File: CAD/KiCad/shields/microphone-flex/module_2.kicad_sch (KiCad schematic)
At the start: 1 part, among them J3 RIGHT / 1x05 RIGHT ANGLE

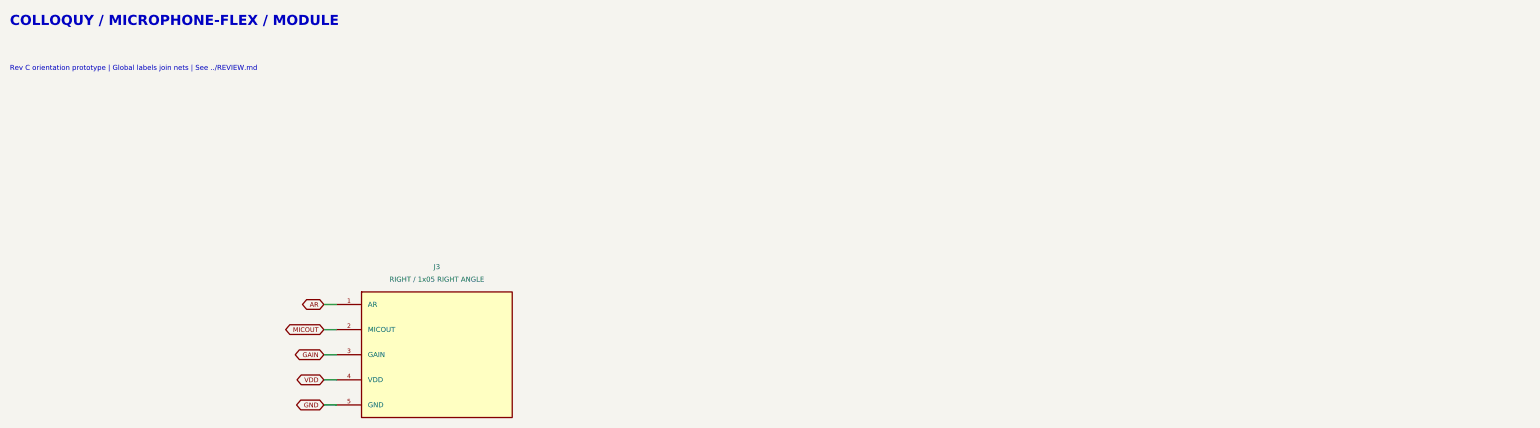
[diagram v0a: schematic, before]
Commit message: Restore removable microphone gain and A/R selectors across flex design
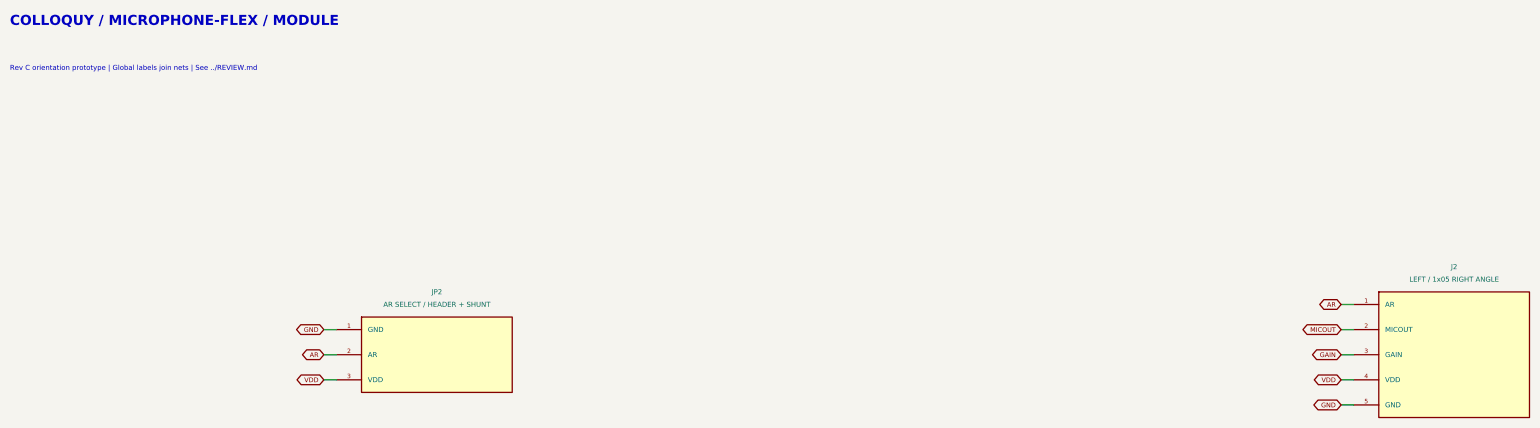
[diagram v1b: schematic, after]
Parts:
- removed J3: RIGHT / 1x05 RIGHT ANGLE, Shields:Flex_Socket_Side, symbol Colloquy:J3
- added J2: LEFT / 1x05 RIGHT ANGLE, Shields:Flex_Socket_Side, symbol Colloquy:J2
- added JP2: AR SELECT / HEADER + SHUNT, Shields:Flex_AR_Selector, symbol Colloquy:JP2
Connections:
- net AR: now also J2.1 (AR), JP2.2 (AR)
- net GAIN: now also J2.3 (GAIN)
- net GND: now also J2.5 (GND), JP2.1 (GND)
- net MICOUT: now also J2.2 (MICOUT)
- net VDD: now also J2.4 (VDD), JP2.3 (VDD)
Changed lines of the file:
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@@
 (kicad_sch (version 20250114) (generator "eeschema") (generator_version "9.0")
  (paper "A3")
-          (title_block (title "microphone-flex / module") (date "2026-10-05") (rev "A-prototype")
+          (title_block (title "microphone-flex / module") (date "2026-10-20") (rev "C-jumpers")
             (company "Colloquy of Mobiles") (comment 1 "Prototype: verify harness polarity and sensor values before connection"))
           (text "COLLOQUY / MICROPHONE-FLEX / MODULE" (at 15.24 15.24 0) (effects (font (size 2.032 2.032) (bold yes)) (justify left top)))
 (text "Rev C orientation prototype | Global labels join nets | See ../REVIEW.md" (at 15.24 25.4 0) (effects (font (size 1.016 1.016) ) (justify left top)))
-(symbol (lib_id "Colloquy:J3") (at 101.6000 83.8200 0) (unit 1) (exclude_from_sim no) (in_bom yes) (on_board yes) (dnp no)
-(property "Reference" "J3" (at 101.6000 66.0400 0) (effects (font (size 1.016 1.016))  ))
-(property "Value" "RIGHT / 1x05 RIGHT ANGLE" (at 101.6000 68.5800 0) (effects (font (size 1.016 1.016))  ))
-(property "Footprint" "Shields:Flex_Socket_Side" (at 101.6000 83.8200 0) (effects (font (size 1.27 1.27))  (hide yes)))
+(symbol (lib_id "Colloquy:JP2") (at 101.6000 83.8200 0) (unit 1) (exclude_from_sim no) (in_bom yes) (on_board yes) (dnp no)
+(property "Reference" "JP2" (at 101.6000 71.1200 0) (effects (font (size 1.016 1.016))  ))
+(property "Value" "AR SELECT / HEADER + SHUNT" (at 101.6000 73.6600 0) (effects (font (size 1.016 1.016))  ))
+(property "Footprint" "Shields:Flex_AR_Selector" (at 101.6000 83.8200 0) (effects (font (size 1.27 1.27))  (hide yes)))
 (property "Datasheet" "" (at 101.6000 83.8200 0) (effects (font (size 1.27 1.27))  (hide yes)))
-(property "Description" "Alternative socket; AR / Out / Gain / Vdd / GND in physical pad order. One module only." (at 101.6000 83.8200 0) (effects (font (size 1.27 1.27))  (hide yes)))
+(property "Description" "Removable 2.54mm selector. 1-2:1:500; 2-3:1:2000; open:1:4000. Initially 1-2. Power off before moving the shunt." (at 101.6000 83.8200 0) (effects (font (size 1.27 1.27))  (hide yes)))
+(pin "1")
+(pin "2")
+(pin "3")
+(instances (project "microphone-flex" (path "/767eeb75-0bc5-5c78-a7ae-aa35b79c1dd4/2d8114f0-91f1-5f81-b7b6-783b8e2a941e" (reference "JP2") (unit 1)))))
+(wire (pts (xy 81.2800 78.7400) (xy 78.7400 78.7400)) (stroke (width 0) (type default)))
+(global_label "GND" (shape bidirectional) (at 78.7400 78.7400 180) (effects (font (size 0.95 0.95)) (justify right)) (property "Intersheetrefs" "${INTERSHEET_REFS}" (at 78.7400 78.7400 0) (effects (font (size 1.016 1.016))  (hide yes))))
+(wire (pts (xy 81.2800 83.8200) (xy 78.7400 83.8200)) (stroke (width 0) (type default)))
+(global_label "AR" (shape bidirectional) (at 78.7400 83.8200 180) (effects (font (size 0.95 0.95)) (justify right)) (property "Intersheetrefs" "${INTERSHEET_REFS}" (at 78.7400 83.8200 0) (effects (font (size 1.016 1.016))  (hide yes))))
+(wire (pts (xy 81.2800 88.9000) (xy 78.7400 88.9000)) (stroke (width 0) (type default)))
+(global_label "VDD" (shape bidirectional) (at 78.7400 88.9000 180) (effects (font (size 0.95 0.95)) (justify right)) (property "Intersheetrefs" "${INTERSHEET_REFS}" (at 78.7400 88.9000 0) (effects (font (size 1.016 1.016))  (hide yes))))
+(symbol (lib_id "Colloquy:J2") (at 307.3400 83.8200 0) (unit 1) (exclude_from_sim no) (in_bom yes) (on_board yes) (dnp no)
+(property "Reference" "J2" (at 307.3400 66.0400 0) (effects (font (size 1.016 1.016))  ))
+(property "Value" "LEFT / 1x05 RIGHT ANGLE" (at 307.3400 68.5800 0) (effects (font (size 1.016 1.016))  ))
+(property "Footprint" "Shields:Flex_Socket_Side" (at 307.3400 83.8200 0) (effects (font (size 1.27 1.27))  (hide yes)))
+(property "Datasheet" "" (at 307.3400 83.8200 0) (effects (font (size 1.27 1.27))  (hide yes)))
+(property "Description" "Alternative socket; AR / Out / Gain / Vdd / GND in physical pad order. One module only." (at 307.3400 83.8200 0) (effects (font (size 1.27 1.27))  (hide yes)))
 (pin "1")
 (pin "2")
@@
 (pin "4")
 (pin "5")
-(instances (project "microphone-flex" (path "/767eeb75-0bc5-5c78-a7ae-aa35b79c1dd4/2d8114f0-91f1-5f81-b7b6-783b8e2a941e" (reference "J3") (unit 1)))))
-(wire (pts (xy 81.2800 73.6600) (xy 78.7400 73.6600)) (stroke (width 0) (type default)))
-(global_label "AR" (shape bidirectional) (at 78.7400 73.6600 180) (effects (font (size 0.95 0.95)) (justify right)) (property "Intersheetrefs" "${INTERSHEET_REFS}" (at 78.7400 73.6600 0) (effects (font (size 1.016 1.016))  (hide yes))))
-(wire (pts (xy 81.2800 78.7400) (xy 78.7400 78.7400)) (stroke (width 0) (type default)))
-(global_label "MICOUT" (shape bidirectional) (at 78.7400 78.7400 180) (effects (font (size 0.95 0.95)) (justify right)) (property "Intersheetrefs" "${INTERSHEET_REFS}" (at 78.7400 78.7400 0) (effects (font (size 1.016 1.016))  (hide yes))))
-(wire (pts (xy 81.2800 83.8200) (xy 78.7400 83.8200)) (stroke (width 0) (type default)))
-(global_label "GAIN" (shape bidirectional) (at 78.7400 83.8200 180) (effects (font (size 0.95 0.95)) (justify right)) (property "Intersheetrefs" "${INTERSHEET_REFS}" (at 78.7400 83.8200 0) (effects (font (size 1.016 1.016))  (hide yes))))
-(wire (pts (xy 81.2800 88.9000) (xy 78.7400 88.9000)) (stroke (width 0) (type default)))
-(global_label "VDD" (shape bidirectional) (at 78.7400 88.9000 180) (effects (font (size 0.95 0.95)) (justify right)) (property "Intersheetrefs" "${INTERSHEET_REFS}" (at 78.7400 88.9000 0) (effects (font (size 1.016 1.016))  (hide yes))))
-(wire (pts (xy 81.2800 93.9800) (xy 78.7400 93.9800)) (stroke (width 0) (type default)))
-(global_label "GND" (shape bidirectional) (at 78.7400 93.9800 180) (effects (font (size 0.95 0.95)) (justify right)) (property "Intersheetrefs" "${INTERSHEET_REFS}" (at 78.7400 93.9800 0) (effects (font (size 1.016 1.016))  (hide yes))))
+(instances (project "microphone-flex" (path "/767eeb75-0bc5-5c78-a7ae-aa35b79c1dd4/2d8114f0-91f1-5f81-b7b6-783b8e2a941e" (reference "J2") (unit 1)))))
+(wire (pts (xy 287.0200 73.6600) (xy 284.4800 73.6600)) (stroke (width 0) (type default)))
+(global_label "AR" (shape bidirectional) (at 284.4800 73.6600 180) (effects (font (size 0.95 0.95)) (justify right)) (property "Intersheetrefs" "${INTERSHEET_REFS}" (at 284.4800 73.6600 0) (effects (font (size 1.016 1.016))  (hide yes))))
+(wire (pts (xy 287.0200 78.7400) (xy 284.4800 78.7400)) (stroke (width 0) (type default)))
+(global_label "MICOUT" (shape bidirectional) (at 284.4800 78.7400 180) (effects (font (size 0.95 0.95)) (justify right)) (property "Intersheetrefs" "${INTERSHEET_REFS}" (at 284.4800 78.7400 0) (effects (font (size 1.016 1.016))  (hide yes))))
+(wire (pts (xy 287.0200 83.8200) (xy 284.4800 83.8200)) (stroke (width 0) (type default)))
+(global_label "GAIN" (shape bidirectional) (at 284.4800 83.8200 180) (effects (font (size 0.95 0.95)) (justify right)) (property "Intersheetrefs" "${INTERSHEET_REFS}" (at 284.4800 83.8200 0) (effects (font (size 1.016 1.016))  (hide yes))))
+(wire (pts (xy 287.0200 88.9000) (xy 284.4800 88.9000)) (stroke (width 0) (type default)))
+(global_label "VDD" (shape bidirectional) (at 284.4800 88.9000 180) (effects (font (size 0.95 0.95)) (justify right)) (property "Intersheetrefs" "${INTERSHEET_REFS}" (at 284.4800 88.9000 0) (effects (font (size 1.016 1.016))  (hide yes))))
+(wire (pts (xy 287.0200 93.9800) (xy 284.4800 93.9800)) (stroke (width 0) (type default)))
+(global_label "GND" (shape bidirectional) (at 284.4800 93.9800 180) (effects (font (size 0.95 0.95)) (justify right)) (property "Intersheetrefs" "${INTERSHEET_REFS}" (at 284.4800 93.9800 0) (effects (font (size 1.016 1.016))  (hide yes))))
           (embedded_fonts no))

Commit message: Reroute microphone flex around the approved component placement
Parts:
- J2: footprint Shields:Flex_Socket_Side -> Shields:Flex_Socket_Left_Overhang
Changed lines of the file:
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@@
 (property "Reference" "J2" (at 307.3400 66.0400 0) (effects (font (size 1.016 1.016))  ))
 (property "Value" "LEFT / 1x05 RIGHT ANGLE" (at 307.3400 68.5800 0) (effects (font (size 1.016 1.016))  ))
-(property "Footprint" "Shields:Flex_Socket_Side" (at 307.3400 83.8200 0) (effects (font (size 1.27 1.27))  (hide yes)))
+(property "Footprint" "Shields:Flex_Socket_Left_Overhang" (at 307.3400 83.8200 0) (effects (font (size 1.27 1.27))  (hide yes)))
 (property "Datasheet" "" (at 307.3400 83.8200 0) (effects (font (size 1.27 1.27))  (hide yes)))
 (property "Description" "Alternative socket; AR / Out / Gain / Vdd / GND in physical pad order. One module only." (at 307.3400 83.8200 0) (effects (font (size 1.27 1.27))  (hide yes)))

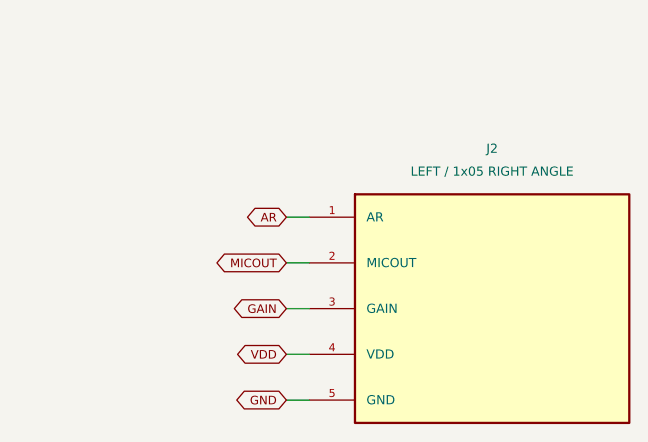
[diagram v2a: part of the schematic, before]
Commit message: Flip side microphones below the carrier and reverse their pin mapping
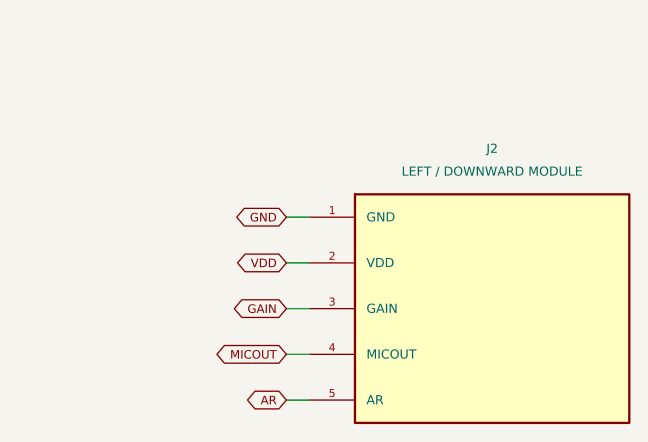
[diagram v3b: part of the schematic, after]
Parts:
- J2: value LEFT / 1x05 RIGHT ANGLE -> LEFT / DOWNWARD MODULE
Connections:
- net AR: now also J2.5 (AR); no longer J2.1 (AR)
- net GND: now also J2.1 (GND); no longer J2.5 (GND)
- net MICOUT: now also J2.4 (MICOUT); no longer J2.2 (MICOUT)
- net VDD: now also J2.2 (VDD); no longer J2.4 (VDD)
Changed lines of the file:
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@@
 (symbol (lib_id "Colloquy:J2") (at 307.3400 83.8200 0) (unit 1) (exclude_from_sim no) (in_bom yes) (on_board yes) (dnp no)
 (property "Reference" "J2" (at 307.3400 66.0400 0) (effects (font (size 1.016 1.016))  ))
-(property "Value" "LEFT / 1x05 RIGHT ANGLE" (at 307.3400 68.5800 0) (effects (font (size 1.016 1.016))  ))
+(property "Value" "LEFT / DOWNWARD MODULE" (at 307.3400 68.5800 0) (effects (font (size 1.016 1.016))  ))
 (property "Footprint" "Shields:Flex_Socket_Left_Overhang" (at 307.3400 83.8200 0) (effects (font (size 1.27 1.27))  (hide yes)))
 (property "Datasheet" "" (at 307.3400 83.8200 0) (effects (font (size 1.27 1.27))  (hide yes)))
-(property "Description" "Alternative socket; AR / Out / Gain / Vdd / GND in physical pad order. One module only." (at 307.3400 83.8200 0) (effects (font (size 1.27 1.27))  (hide yes)))
+(property "Description" "Side module hangs below the PCB, rotated 180 degrees about the insertion axis. GND / Vdd / Gain / Out / AR in physical pad order. One module only." (at 307.3400 83.8200 0) (effects (font (size 1.27 1.27))  (hide yes)))
 (pin "1")
 (pin "2")
@@
 (instances (project "microphone-flex" (path "/767eeb75-0bc5-5c78-a7ae-aa35b79c1dd4/2d8114f0-91f1-5f81-b7b6-783b8e2a941e" (reference "J2") (unit 1)))))
 (wire (pts (xy 287.0200 73.6600) (xy 284.4800 73.6600)) (stroke (width 0) (type default)))
-(global_label "AR" (shape bidirectional) (at 284.4800 73.6600 180) (effects (font (size 0.95 0.95)) (justify right)) (property "Intersheetrefs" "${INTERSHEET_REFS}" (at 284.4800 73.6600 0) (effects (font (size 1.016 1.016))  (hide yes))))
+(global_label "GND" (shape bidirectional) (at 284.4800 73.6600 180) (effects (font (size 0.95 0.95)) (justify right)) (property "Intersheetrefs" "${INTERSHEET_REFS}" (at 284.4800 73.6600 0) (effects (font (size 1.016 1.016))  (hide yes))))
 (wire (pts (xy 287.0200 78.7400) (xy 284.4800 78.7400)) (stroke (width 0) (type default)))
-(global_label "MICOUT" (shape bidirectional) (at 284.4800 78.7400 180) (effects (font (size 0.95 0.95)) (justify right)) (property "Intersheetrefs" "${INTERSHEET_REFS}" (at 284.4800 78.7400 0) (effects (font (size 1.016 1.016))  (hide yes))))
+(global_label "VDD" (shape bidirectional) (at 284.4800 78.7400 180) (effects (font (size 0.95 0.95)) (justify right)) (property "Intersheetrefs" "${INTERSHEET_REFS}" (at 284.4800 78.7400 0) (effects (font (size 1.016 1.016))  (hide yes))))
 (wire (pts (xy 287.0200 83.8200) (xy 284.4800 83.8200)) (stroke (width 0) (type default)))
 (global_label "GAIN" (shape bidirectional) (at 284.4800 83.8200 180) (effects (font (size 0.95 0.95)) (justify right)) (property "Intersheetrefs" "${INTERSHEET_REFS}" (at 284.4800 83.8200 0) (effects (font (size 1.016 1.016))  (hide yes))))
 (wire (pts (xy 287.0200 88.9000) (xy 284.4800 88.9000)) (stroke (width 0) (type default)))
-(global_label "VDD" (shape bidirectional) (at 284.4800 88.9000 180) (effects (font (size 0.95 0.95)) (justify right)) (property "Intersheetrefs" "${INTERSHEET_REFS}" (at 284.4800 88.9000 0) (effects (font (size 1.016 1.016))  (hide yes))))
+(global_label "MICOUT" (shape bidirectional) (at 284.4800 88.9000 180) (effects (font (size 0.95 0.95)) (justify right)) (property "Intersheetrefs" "${INTERSHEET_REFS}" (at 284.4800 88.9000 0) (effects (font (size 1.016 1.016))  (hide yes))))
 (wire (pts (xy 287.0200 93.9800) (xy 284.4800 93.9800)) (stroke (width 0) (type default)))
-(global_label "GND" (shape bidirectional) (at 284.4800 93.9800 180) (effects (font (size 0.95 0.95)) (justify right)) (property "Intersheetrefs" "${INTERSHEET_REFS}" (at 284.4800 93.9800 0) (effects (font (size 1.016 1.016))  (hide yes))))
+(global_label "AR" (shape bidirectional) (at 284.4800 93.9800 180) (effects (font (size 0.95 0.95)) (justify right)) (property "Intersheetrefs" "${INTERSHEET_REFS}" (at 284.4800 93.9800 0) (effects (font (size 1.016 1.016))  (hide yes))))
           (embedded_fonts no))
